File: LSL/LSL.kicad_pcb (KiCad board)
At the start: 2 copper layers, 61 x 26.7 mm, 11 parts, among them J1 Conn_01x01_Male, J2 Conn_01x08_Male, J3 Conn_01x08_Male, J4 Conn_01x01_Male, J5 Conn_01x05_Male, U1 74HC00, U2 74LS573

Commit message: Fix text & date
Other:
- board text added: "11.12.2022"
- board text removed: "26.11.2022"
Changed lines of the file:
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@@
   (general
     (thickness 1.6)
-    (drawings 22)
+    (drawings 23)
     (tracks 180)
     (zones 0)
@@
   )
   (setup
-    (last_trace_width 0.5)
+    (last_trace_width 0.25)
     (user_trace_width 0.4)
     (user_trace_width 0.5)
@@
     )
   )
+  (gr_text LSL (at 69.215 50.165) (layer F.Cu)
+    (effects (font (size 3 3) (thickness 0.5)))
+  )
   (gr_circle (center 115.57 47.625) (end 115.97 47.625) (layer F.Cu) (width 0.2))
   (gr_circle (center 100.33 47.625) (end 100.73 47.625) (layer F.Cu) (width 0.2))
@@
     (effects (font (size 1 1) (thickness 0.15)))
   )
-  (gr_text Gnd (at 116.84 60.96 90) (layer F.SilkS)
+  (gr_text Gnd (at 116.84 60.96) (layer F.SilkS)
     (effects (font (size 1 1) (thickness 0.15)))
   )
@@
     (effects (font (size 1 1) (thickness 0.15)))
   )
-  (gr_text 26.11.2022 (at 71.755 45.085) (layer F.Cu)
+  (gr_text 11.12.2022 (at 71.755 45.085) (layer F.Cu)
     (effects (font (size 1.5 1.5) (thickness 0.3)))
   )
-  (gr_text LSL (at 74.93 50.165) (layer F.SilkS)
+  (gr_text LSL (at 69.215 50.165) (layer F.SilkS)
     (effects (font (size 3 3) (thickness 0.5)))
   )

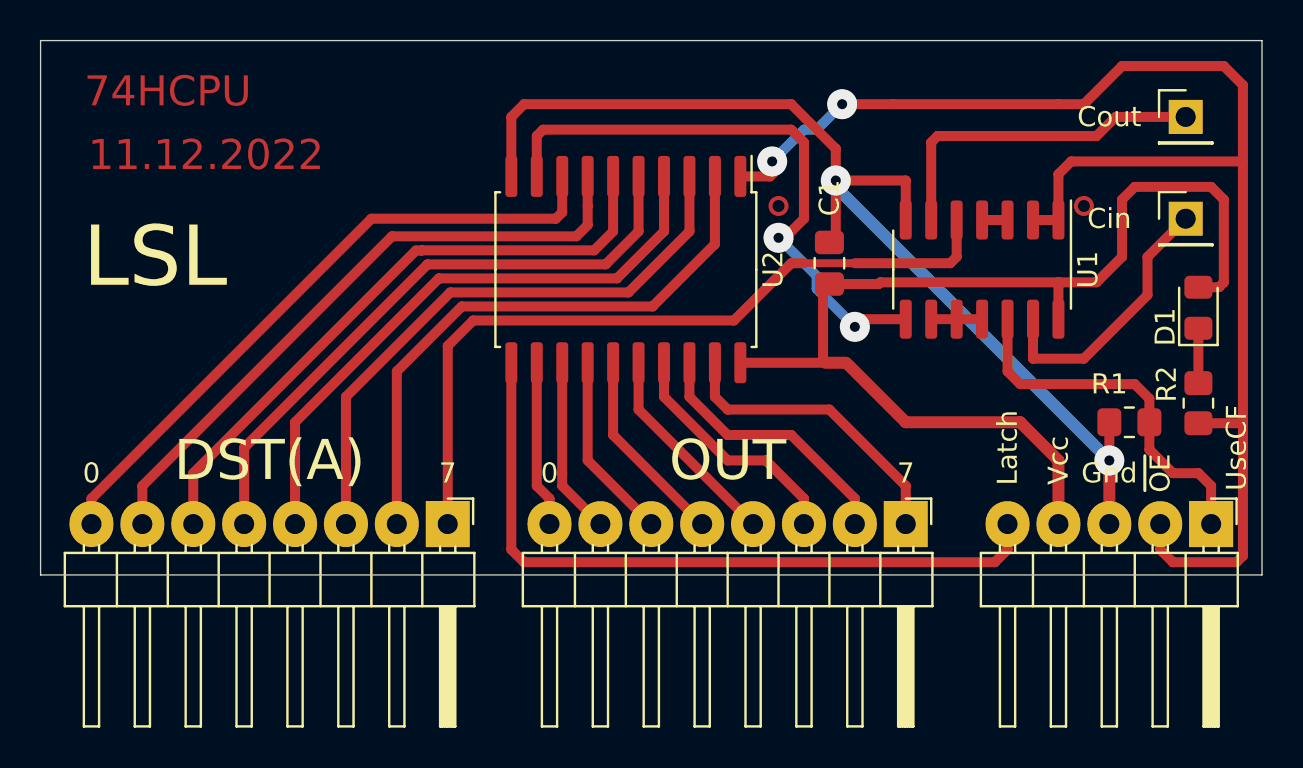
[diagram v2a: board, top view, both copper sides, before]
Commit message: Swap OE & UseCF pins
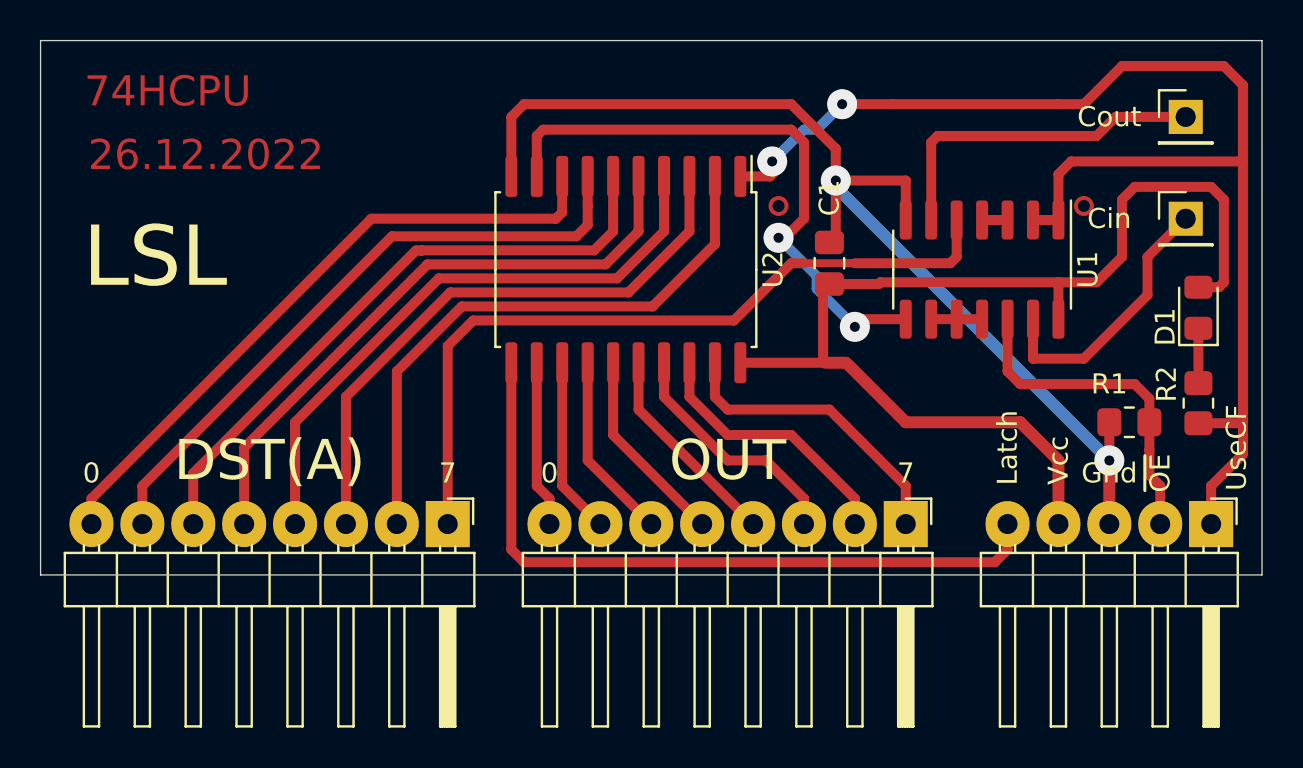
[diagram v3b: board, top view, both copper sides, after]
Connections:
- J5 pad 1: /UseCF -> /~OE
- J5 pad 2: /~OE -> /UseCF
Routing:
- net /~OE: track 72.7 -> 66.0 mm
- net /UseCF: track 18.5 -> 16.7 mm
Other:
- board text added: "26.12.2022"
- board text removed: "11.12.2022"
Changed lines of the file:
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@@
     (thickness 1.6)
     (drawings 23)
-    (tracks 180)
+    (tracks 177)
     (zones 0)
     (modules 11)
@@
     (visible_elements 7FFFFFFF)
     (pcbplotparams
-      (layerselection 0x010fc_ffffffff)
+      (layerselection 0x00000_7fffffff)
       (usegerberextensions false)
       (usegerberattributes true)
@@
       (hpglpenspeed 20)
       (hpglpendiameter 15.000000)
-      (psnegative false)
+      (psnegative true)
       (psa4output false)
       (plotreference true)
@@
       (padsonsilk false)
       (subtractmaskfromsilk false)
-      (outputformat 1)
-      (mirror false)
+      (outputformat 4)
+      (mirror true)
       (drillshape 1)
       (scaleselection 1)
-      (outputdirectory ""))
+      (outputdirectory "pdf/"))
   )
   (net 0 "")
@@
       (net 2 GND))
     (pad 2 thru_hole oval (at 0 2.54 270) (size 2.3 2.2) (drill 1) (layers *.Cu *.Mask)
+      (net 22 /UseCF))
+    (pad 1 thru_hole rect (at 0 0 270) (size 2.3 2.2) (drill 1) (layers *.Cu *.Mask)
       (net 23 /~OE))
-    (pad 1 thru_hole rect (at 0 0 270) (size 2.3 2.2) (drill 1) (layers *.Cu *.Mask)
-      (net 22 /UseCF))
     (model ${KISYS3DMOD}/Connector_PinHeader_2.54mm.3dshapes/PinHeader_1x05_P2.54mm_Horizontal.wrl
       (at (xyz 0 0 0))
@@
       (effects (font (size 0.5 0.5) (thickness 0.08)))
     )
-    (pad 1 smd roundrect (at -1.0375 0 90) (size 1.175 1.45) (layers F.Cu F.Paste F.Mask) (roundrect_rratio 0.212766)
+    (pad 1 smd roundrect (at -1.0375 0 90) (size 1.175 1.45) (layers F.Cu F.Paste F.Mask) (roundrect_rratio 0.2127659574468085)
       (net 1 VCC))
-    (pad 2 smd roundrect (at 1.0375 0 90) (size 1.175 1.45) (layers F.Cu F.Paste F.Mask) (roundrect_rratio 0.212766)
+    (pad 2 smd roundrect (at 1.0375 0 90) (size 1.175 1.45) (layers F.Cu F.Paste F.Mask) (roundrect_rratio 0.2127659574468085)
       (net 2 GND))
     (model ${KISYS3DMOD}/Capacitor_SMD.3dshapes/C_0805_2012Metric.wrl
@@
       (effects (font (size 0.5 0.5) (thickness 0.08)))
     )
-    (pad 1 smd roundrect (at -1.025 0 90) (size 1.15 1.4) (layers F.Cu F.Paste F.Mask) (roundrect_rratio 0.217391)
+    (pad 1 smd roundrect (at -1.025 0 90) (size 1.15 1.4) (layers F.Cu F.Paste F.Mask) (roundrect_rratio 0.2173904347826087)
       (net 3 "Net-(D1-Pad1)"))
-    (pad 2 smd roundrect (at 1.025 0 90) (size 1.15 1.4) (layers F.Cu F.Paste F.Mask) (roundrect_rratio 0.217391)
+    (pad 2 smd roundrect (at 1.025 0 90) (size 1.15 1.4) (layers F.Cu F.Paste F.Mask) (roundrect_rratio 0.2173904347826087)
       (net 1 VCC))
     (model ${KISYS3DMOD}/LED_SMD.3dshapes/LED_0805_2012Metric.wrl
@@
       (effects (font (size 0.5 0.5) (thickness 0.08)))
     )
-    (pad 2 smd roundrect (at 1 0 180) (size 1.2 1.4) (layers F.Cu F.Paste F.Mask) (roundrect_rratio 0.208333)
+    (pad 2 smd roundrect (at 1 0 180) (size 1.2 1.4) (layers F.Cu F.Paste F.Mask) (roundrect_rratio 0.2083325)
       (net 2 GND))
-    (pad 1 smd roundrect (at -1 0 180) (size 1.2 1.4) (layers F.Cu F.Paste F.Mask) (roundrect_rratio 0.208333)
+    (pad 1 smd roundrect (at -1 0 180) (size 1.2 1.4) (layers F.Cu F.Paste F.Mask) (roundrect_rratio 0.2083325)
       (net 22 /UseCF))
     (model ${KISYS3DMOD}/Resistor_SMD.3dshapes/R_0805_2012Metric.wrl
@@
       (effects (font (size 0.5 0.5) (thickness 0.08)))
     )
-    (pad 1 smd roundrect (at -1 0 270) (size 1.2 1.4) (layers F.Cu F.Paste F.Mask) (roundrect_rratio 0.208333)
+    (pad 1 smd roundrect (at -1 0 270) (size 1.2 1.4) (layers F.Cu F.Paste F.Mask) (roundrect_rratio 0.2083325)
       (net 3 "Net-(D1-Pad1)"))
-    (pad 2 smd roundrect (at 1 0 270) (size 1.2 1.4) (layers F.Cu F.Paste F.Mask) (roundrect_rratio 0.208333)
+    (pad 2 smd roundrect (at 1 0 270) (size 1.2 1.4) (layers F.Cu F.Paste F.Mask) (roundrect_rratio 0.2083325)
       (net 23 /~OE))
     (model ${KISYS3DMOD}/Resistor_SMD.3dshapes/R_0805_2012Metric.wrl
@@
     (effects (font (size 1 1) (thickness 0.15)))
   )
-  (gr_text 11.12.2022 (at 71.755 45.085) (layer F.Cu)
+  (gr_text 26.12.2022 (at 71.755 45.085) (layer F.Cu)
     (effects (font (size 1.5 1.5) (thickness 0.3)))
   )
@@
   (segment (start 113.03 55.245) (end 115.57 55.245) (width 0.5) (layer F.Cu) (net 21))
   (segment (start 113.03 53.275) (end 113.03 55.245) (width 0.5) (layer F.Cu) (net 21) (status 10))
-  (segment (start 121.92 61.595) (end 121.92 63.5) (width 0.5) (layer F.Cu) (net 22) (status 20))
-  (segment (start 121.285 60.96) (end 121.92 61.595) (width 0.5) (layer F.Cu) (net 22))
-  (segment (start 120.015 60.96) (end 121.285 60.96) (width 0.5) (layer F.Cu) (net 22))
-  (segment (start 118.84 59.785) (end 120.015 60.96) (width 0.5) (layer F.Cu) (net 22))
   (segment (start 118.84 58.42) (end 118.84 59.785) (width 0.5) (layer F.Cu) (net 22) (status 10))
   (segment (start 118.84 57.245) (end 118.84 58.42) (width 0.5) (layer F.Cu) (net 22) (status 20))
@@
   (segment (start 111.76 55.88) (end 112.395 56.515) (width 0.5) (layer F.Cu) (net 22))
   (segment (start 111.76 53.275) (end 111.76 55.88) (width 0.5) (layer F.Cu) (net 22) (status 10))
-  (segment (start 119.38 64.77) (end 119.38 63.5) (width 0.5) (layer F.Cu) (net 23) (status 20))
-  (segment (start 120.015 65.405) (end 119.38 64.77) (width 0.5) (layer F.Cu) (net 23))
-  (segment (start 123.19 65.405) (end 120.015 65.405) (width 0.5) (layer F.Cu) (net 23))
-  (segment (start 123.5075 65.0875) (end 123.19 65.405) (width 0.5) (layer F.Cu) (net 23))
+  (segment (start 119.38 63.5) (end 119.38 61.595) (width 0.5) (layer F.Cu) (net 22))
+  (segment (start 118.84 61.055) (end 118.84 59.785) (width 0.5) (layer F.Cu) (net 22))
+  (segment (start 119.38 61.595) (end 118.84 61.055) (width 0.5) (layer F.Cu) (net 22))
+  (segment (start 121.92 61.595) (end 121.92 63.5) (width 0.5) (layer F.Cu) (net 23) (status 20))
   (segment (start 113.03 48.325) (end 114.3 48.325) (width 0.5) (layer F.Cu) (net 23) (status 30))
   (via (at 103.505 42.545) (size 1.5) (drill 0.5) (layers F.Cu B.Cu) (net 23))
   (segment (start 123.46 58.4675) (end 123.5075 58.42) (width 0.5) (layer F.Cu) (net 23))
   (segment (start 121.285 58.4675) (end 123.46 58.4675) (width 0.5) (layer F.Cu) (net 23) (status 10))
-  (segment (start 123.5075 58.42) (end 123.5075 65.0875) (width 0.5) (layer F.Cu) (net 23))
   (segment (start 114.3 42.545) (end 106.045 42.545) (width 0.5) (layer F.Cu) (net 23))
   (segment (start 115.57 42.545) (end 114.3 42.545) (width 0.5) (layer F.Cu) (net 23))
@@
   (segment (start 101.6 43.815) (end 100.0125 45.4025) (width 0.5) (layer B.Cu) (net 23))
   (segment (start 102.235 43.815) (end 101.6 43.815) (width 0.5) (layer B.Cu) (net 23))
+  (segment (start 121.92 61.595) (end 123.5075 60.0075) (width 0.5) (layer F.Cu) (net 23))
+  (segment (start 123.5075 58.42) (end 123.5075 60.0075) (width 0.5) (layer F.Cu) (net 23))
   (segment (start 111.76 64.77) (end 111.76 63.5) (width 0.5) (layer F.Cu) (net 24) (status 20))
   (segment (start 111.125 65.405) (end 111.76 64.77) (width 0.5) (layer F.Cu) (net 24))
